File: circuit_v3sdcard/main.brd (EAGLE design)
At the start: 28 x 47 mm, 30 parts, among them CN1 SD, CN2 USB_BARE, CN3 MICROSD, IC1 C8051F381-GM, IC3 N25Q512A, IC4 KC2016K, IC6 MPU-9250, P0.0 PTR1TP10R, SW2 PTR1TP10R

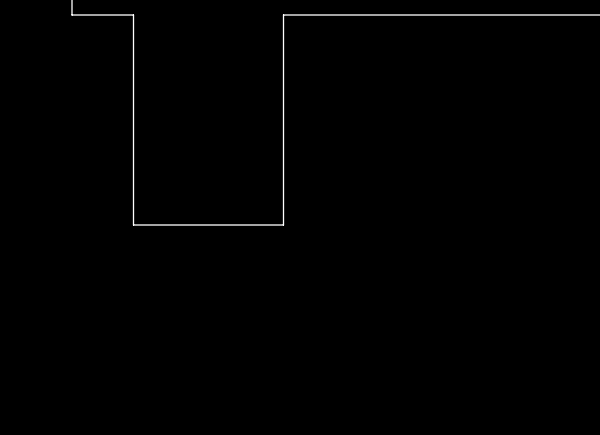
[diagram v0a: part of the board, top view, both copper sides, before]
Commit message: Added molex connector's library
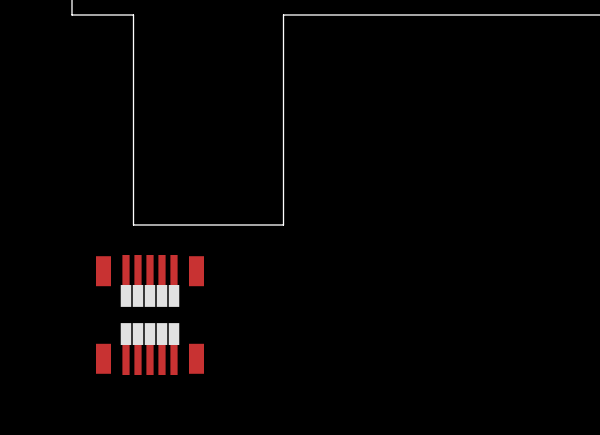
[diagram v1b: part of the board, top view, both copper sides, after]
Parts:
- added CN4: 5035481020, Connector:5035481020
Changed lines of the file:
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@@
 <element name="CN1" library="Connector" package="SD" value="SD" x="20.17" y="23.67" rot="MR0"/>
 <element name="CN3" library="Connector" package="BLOCK_SD_CONNECTOR" value="MICROSD" x="16" y="9"/>
+<element name="CN4" library="Connector" package="5035481020" value="5035481020" x="3" y="-3"/>
 </elements>
 <signals>

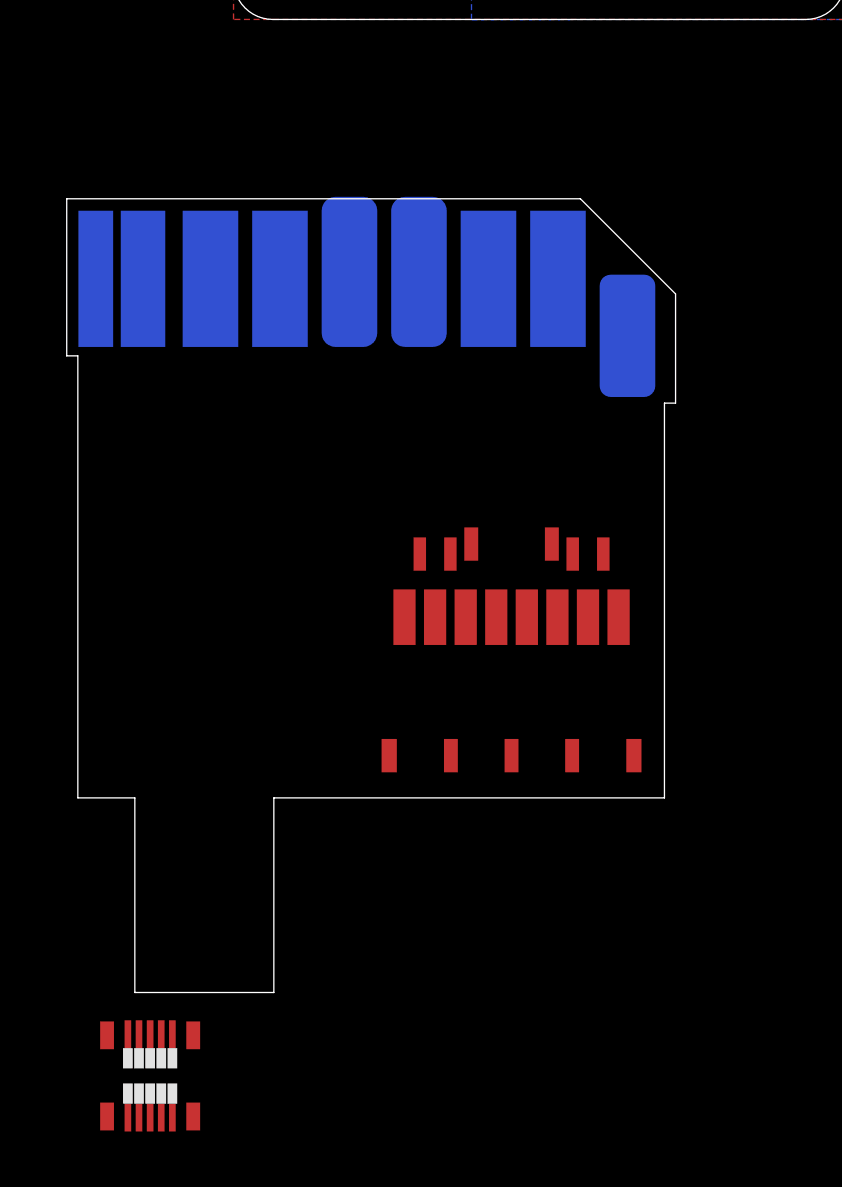
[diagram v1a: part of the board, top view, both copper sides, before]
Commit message: Modified Contours
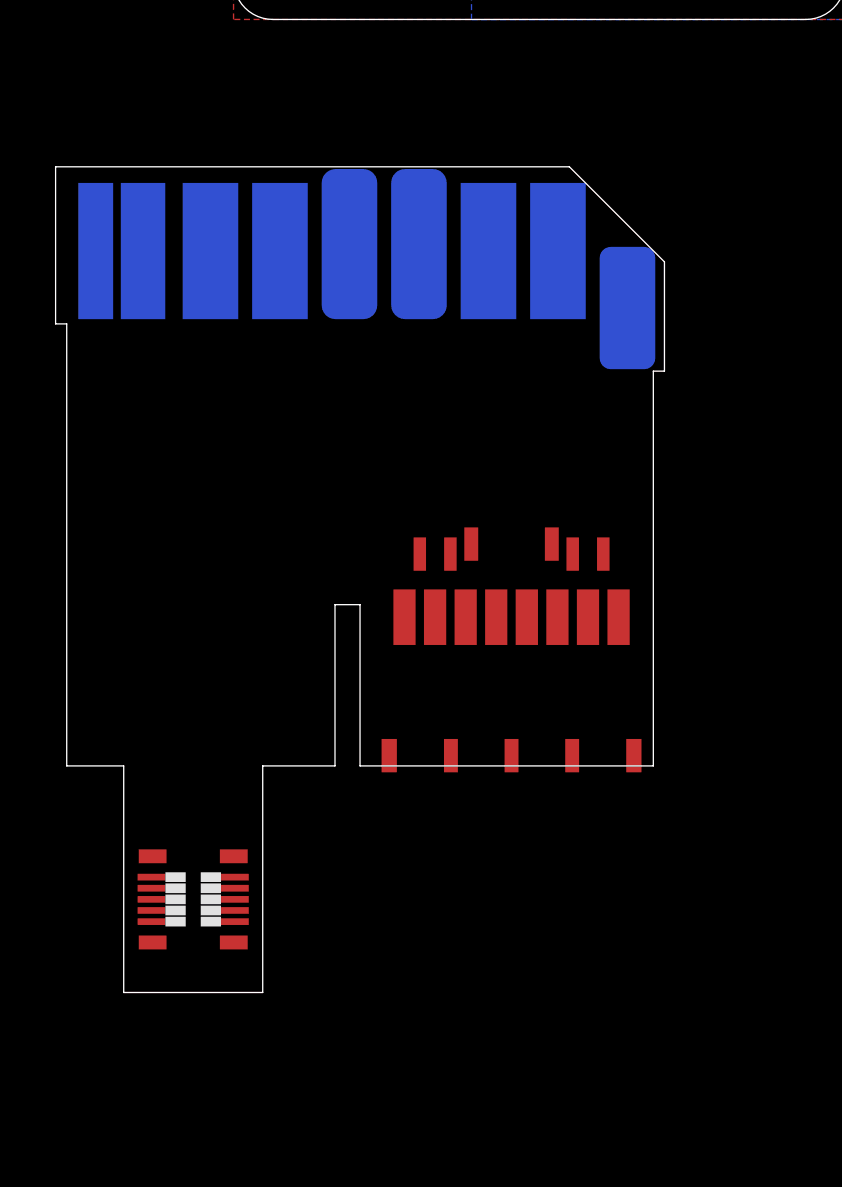
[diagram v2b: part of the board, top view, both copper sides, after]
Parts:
- moved CN4 6.54 mm to (4.55, 3.35), turned to 90 degrees
- moved CN1 1.00 mm to (20.2, 24.7)
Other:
- board size 28 x 47 mm -> 28.4 x 47 mm
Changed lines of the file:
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@@
 <text x="14.4" y="38.39" size="0.8128" layer="26" font="vector" ratio="12" rot="SMR0">Designed by</text>
 <text x="14.44" y="35.89" size="0.8128" layer="26" font="vector" ratio="12" rot="SMR0">Y. Sato</text>
-<wire x1="2.45" y1="0" x2="2.45" y2="7" width="0" layer="20"/>
-<wire x1="2.45" y1="7" x2="0.4" y2="7" width="0" layer="20"/>
-<wire x1="0.4" y1="7" x2="0.4" y2="22.9" width="0" layer="20"/>
-<wire x1="0.4" y1="22.9" x2="0" y2="22.9" width="0" layer="20"/>
-<wire x1="0" y1="22.9" x2="0" y2="28.55" width="0" layer="20"/>
-<wire x1="0" y1="28.55" x2="18.477" y2="28.55" width="0" layer="20"/>
-<wire x1="18.477" y1="28.55" x2="21.9" y2="25.127" width="0" layer="20"/>
-<wire x1="21.9" y1="25.127" x2="21.9" y2="21.2" width="0" layer="20"/>
-<wire x1="21.9" y1="21.2" x2="21.5" y2="21.2" width="0" layer="20"/>
-<wire x1="21.5" y1="21.2" x2="21.5" y2="7" width="0" layer="20"/>
-<wire x1="21.5" y1="7" x2="7.45" y2="7" width="0" layer="20"/>
-<wire x1="7.45" y1="7" x2="7.45" y2="0" width="0" layer="20"/>
-<wire x1="7.45" y1="0" x2="2.45" y2="0" width="0" layer="20"/>
+<wire x1="2.05" y1="0" x2="2.05" y2="8.15" width="0" layer="20"/>
+<wire x1="2.05" y1="8.15" x2="0" y2="8.15" width="0" layer="20"/>
+<wire x1="0" y1="8.15" x2="0" y2="24.05" width="0" layer="20"/>
+<wire x1="0" y1="24.05" x2="-0.4" y2="24.05" width="0" layer="20"/>
+<wire x1="-0.4" y1="24.05" x2="-0.4" y2="29.7" width="0" layer="20"/>
+<wire x1="-0.4" y1="29.7" x2="18.08" y2="29.7" width="0" layer="20"/>
+<wire x1="18.08" y1="29.7" x2="21.5" y2="26.28" width="0" layer="20"/>
+<wire x1="21.5" y1="26.28" x2="21.5" y2="22.35" width="0" layer="20"/>
+<wire x1="21.5" y1="22.35" x2="21.1" y2="22.35" width="0" layer="20"/>
+<wire x1="21.1" y1="22.35" x2="21.1" y2="8.15" width="0" layer="20"/>
+<wire x1="21.1" y1="8.15" x2="10.55" y2="8.15" width="0" layer="20"/>
+<wire x1="9.65" y1="8.15" x2="7.05" y2="8.15" width="0" layer="20"/>
+<wire x1="7.05" y1="8.15" x2="7.05" y2="0" width="0" layer="20"/>
+<wire x1="7.05" y1="0" x2="2.05" y2="0" width="0" layer="20"/>
+<wire x1="10.55" y1="8.15" x2="10.55" y2="13.95" width="0" layer="20"/>
+<wire x1="10.55" y1="13.95" x2="9.65" y2="13.95" width="0" layer="20"/>
+<wire x1="9.65" y1="13.95" x2="9.65" y2="8.15" width="0" layer="20"/>
 </plain>
 <attributes>
@@
 <attribute name="VALUE" x="21.615" y="41.225" size="1.27" layer="28" rot="MR0"/>
 </element>
-<element name="CN1" library="Connector" package="SD" value="SD" x="20.17" y="23.67" rot="MR0"/>
+<element name="CN1" library="Connector" package="SD" value="SD" x="20.17" y="24.67" rot="MR0"/>
 <element name="CN3" library="Connector" package="BLOCK_SD_CONNECTOR" value="MICROSD" x="16" y="9"/>
-<element name="CN4" library="Connector" package="5035481020" value="5035481020" x="3" y="-3"/>
+<element name="CN4" library="Connector" package="5035481020" value="5035481020" x="4.55" y="3.35" rot="R90"/>
 </elements>
 <signals>

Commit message: Modified circuit
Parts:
- moved CN3 0.83 mm to (15.7, 8.23)
- moved CN4 0.50 mm to (4.55, 2.85)
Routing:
- added copper zone on layer 1, net DGND
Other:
- outline, holes or cut-outs redrawn
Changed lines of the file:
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@@
 <text x="14.4" y="38.39" size="0.8128" layer="26" font="vector" ratio="12" rot="SMR0">Designed by</text>
 <text x="14.44" y="35.89" size="0.8128" layer="26" font="vector" ratio="12" rot="SMR0">Y. Sato</text>
-<wire x1="2.05" y1="0" x2="2.05" y2="8.15" width="0" layer="20"/>
-<wire x1="2.05" y1="8.15" x2="0" y2="8.15" width="0" layer="20"/>
-<wire x1="0" y1="8.15" x2="0" y2="24.05" width="0" layer="20"/>
+<wire x1="2.05" y1="0" x2="2.05" y2="7.15" width="0" layer="20"/>
+<wire x1="2.05" y1="7.15" x2="0" y2="7.15" width="0" layer="20"/>
+<wire x1="0" y1="7.15" x2="0" y2="24.05" width="0" layer="20"/>
 <wire x1="0" y1="24.05" x2="-0.4" y2="24.05" width="0" layer="20"/>
 <wire x1="-0.4" y1="24.05" x2="-0.4" y2="29.7" width="0" layer="20"/>
@@
 <wire x1="21.5" y1="26.28" x2="21.5" y2="22.35" width="0" layer="20"/>
 <wire x1="21.5" y1="22.35" x2="21.1" y2="22.35" width="0" layer="20"/>
-<wire x1="21.1" y1="22.35" x2="21.1" y2="8.15" width="0" layer="20"/>
-<wire x1="21.1" y1="8.15" x2="10.55" y2="8.15" width="0" layer="20"/>
-<wire x1="9.65" y1="8.15" x2="7.05" y2="8.15" width="0" layer="20"/>
-<wire x1="7.05" y1="8.15" x2="7.05" y2="0" width="0" layer="20"/>
+<wire x1="21.1" y1="22.35" x2="21.1" y2="6.85" width="0" layer="20"/>
+<wire x1="21.1" y1="6.85" x2="10.7" y2="6.85" width="0" layer="20"/>
+<wire x1="9.65" y1="7.15" x2="7.05" y2="7.15" width="0" layer="20"/>
+<wire x1="7.05" y1="7.15" x2="7.05" y2="0" width="0" layer="20"/>
 <wire x1="7.05" y1="0" x2="2.05" y2="0" width="0" layer="20"/>
-<wire x1="10.55" y1="8.15" x2="10.55" y2="13.95" width="0" layer="20"/>
-<wire x1="10.55" y1="13.95" x2="9.65" y2="13.95" width="0" layer="20"/>
-<wire x1="9.65" y1="13.95" x2="9.65" y2="8.15" width="0" layer="20"/>
+<wire x1="10.7" y1="6.85" x2="10.7" y2="17" width="0" layer="20"/>
+<wire x1="10.7" y1="17" x2="9.65" y2="17" width="0" layer="20"/>
+<wire x1="9.65" y1="17" x2="9.65" y2="7.15" width="0" layer="20"/>
 </plain>
 <attributes>
@@
 </element>
 <element name="CN1" library="Connector" package="SD" value="SD" x="20.17" y="24.67" rot="MR0"/>
-<element name="CN3" library="Connector" package="BLOCK_SD_CONNECTOR" value="MICROSD" x="16" y="9"/>
-<element name="CN4" library="Connector" package="5035481020" value="5035481020" x="4.55" y="3.35" rot="R90"/>
+<element name="CN3" library="Connector" package="BLOCK_SD_CONNECTOR" value="MICROSD" x="15.7" y="8.23"/>
+<element name="CN4" library="Connector" package="5035481020" value="5035481020" x="4.55" y="2.85" rot="R90"/>
 </elements>
 <signals>
@@
 <vertex x="14.56" y="34.99"/>
 </polygon>
+<polygon width="0.1524" layer="1">
+<vertex x="3" y="21"/>
+<vertex x="5" y="19"/>
+<vertex x="5" y="16"/>
+<vertex x="3" y="16"/>
+</polygon>
 </signal>

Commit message: Modified SD circuit
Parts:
- CN1: device Connector:SD -> Connector:SD_V3
- moved CN1 0.24 mm to (19.9, 24.7)
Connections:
- new net N$10: CN1.DI(CMD), CN3.CMD
- new net N$12: CN1.!CS!(DAT3), CN3.CD/DAT3
- new net N$14: CN1.RSV(DAT2), CN3.DAT2
- new net N$2: CN1.RSV(DAT1), CN3.DAT1
- new net N$3: CN1.DO(DAT0), CN3.DAT0
- new net N$4: CN1.VSS1, CN1.VSS2, CN3.VSS
- new net N$6: CN1.SCLK, CN3.CLK
- new net N$8: CN1.VDD, CN3.VDD
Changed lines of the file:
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@@
 <setting verticaltext="up"/>
 </settings>
-<grid distance="1" unitdist="mm" unit="mm" style="lines" multiple="1" display="yes" altdistance="0.01" altunitdist="mm" altunit="mm"/>
+<grid distance="0.5" unitdist="mm" unit="mm" style="lines" multiple="1" display="yes" altdistance="0.01" altunitdist="mm" altunit="mm"/>
 <layers>
 <layer number="1" name="Top" color="4" fill="1" visible="yes" active="yes"/>
@@
 </variantdefs>
 <classes>
-<class number="0" name="default" width="0" drill="0">
+<class number="0" name="signal" width="0.1524" drill="0">
+</class>
+<class number="1" name="power" width="0.254" drill="0">
 </class>
 </classes>
@@
 <attribute name="VALUE" x="21.615" y="41.225" size="1.27" layer="28" rot="MR0"/>
 </element>
-<element name="CN1" library="Connector" package="SD" value="SD" x="20.17" y="24.67" rot="MR0"/>
+<element name="CN1" library="Connector" package="SD_V3" value="SD" x="19.93" y="24.68" rot="MR0"/>
 <element name="CN3" library="Connector" package="BLOCK_SD_CONNECTOR" value="MICROSD" x="15.7" y="8.23"/>
 <element name="CN4" library="Connector" package="5035481020" value="5035481020" x="4.55" y="2.85" rot="R90"/>
@@
 <wire x1="14.255" y1="44.545" x2="14.255" y2="44.3" width="0.1524" layer="1"/>
 </signal>
+<signal name="N$2">
+<contactref element="CN3" pad="DAT1"/>
+<contactref element="CN1" pad="RSV(DAT1)"/>
+<wire x1="11.3" y1="7.8" x2="0.81" y2="26.88" width="0" layer="19" extent="1-16"/>
+</signal>
+<signal name="N$3">
+<contactref element="CN1" pad="DO(DAT0)"/>
+<contactref element="CN3" pad="DAT0"/>
+<wire x1="12.4" y1="15" x2="2.51" y2="26.88" width="0" layer="19" extent="1-16"/>
+</signal>
+<signal name="N$4">
+<contactref element="CN3" pad="VSS"/>
+<contactref element="CN1" pad="VSS2"/>
+<contactref element="CN1" pad="VSS1"/>
+<wire x1="4.93" y1="26.88" x2="12.43" y2="26.98" width="0" layer="19" extent="16-16"/>
+<wire x1="13.5" y1="15" x2="12.43" y2="26.98" width="0" layer="19" extent="1-16"/>
+</signal>
+<signal name="N$6">
+<contactref element="CN1" pad="SCLK"/>
+<contactref element="CN3" pad="CLK"/>
+<wire x1="14.25" y1="15.36" x2="7.43" y2="26.88" width="0" layer="19" extent="1-16"/>
+</signal>
+<signal name="N$8">
+<contactref element="CN3" pad="VDD"/>
+<contactref element="CN1" pad="VDD"/>
+<wire x1="17.15" y1="15.36" x2="9.93" y2="26.98" width="0" layer="19" extent="1-16"/>
+</signal>
+<signal name="N$10">
+<contactref element="CN1" pad="DI(CMD)"/>
+<contactref element="CN3" pad="CMD"/>
+<wire x1="17.9" y1="15" x2="14.93" y2="26.88" width="0" layer="19" extent="1-16"/>
+</signal>
+<signal name="N$12">
+<contactref element="CN1" pad="!CS!(DAT3)"/>
+<contactref element="CN3" pad="CD/DAT3"/>
+<wire x1="17.43" y1="26.88" x2="19" y2="15" width="0" layer="19" extent="1-16"/>
+</signal>
+<signal name="N$14">
+<contactref element="CN3" pad="DAT2"/>
+<contactref element="CN1" pad="RSV(DAT2)"/>
+<wire x1="20.1" y1="7.8" x2="19.93" y2="24.68" width="0" layer="19" extent="1-16"/>
+</signal>
 </signals>

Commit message: Modified v3 circuit
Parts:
- removed C2CK, C2D, DGND, GND, P0.0, SW2: PTR1TP10R, testpad:TP10R
- removed CN2: USB_BARE, Connector:USB_BARE
- removed HDMI_5V, HDMI_GND: PTR1TP11R, testpad:TP11R
- removed R3: 100, reg,cap:1005
- added D4: (no value), diode:SOD323-W
- added TP: PTR1TP10R, testpad:TP10R
- added USB_GND: PTR1TP11R, testpad:TP11R
- R1: value 100k -> 10k
- moved R1 61.5 mm to (1.00, -15.0), flipped to the top
- moved D1 54.7 mm to (2.00, -7.00), flipped to the top
- moved D2 52.8 mm to (2.00, -3.00), flipped to the top, turned to 0 degrees
- moved D3 21.5 mm to (19.0, 19.5), flipped to the top
- moved R7 6.58 mm to (22.0, 30.5), flipped to the top
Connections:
- net IN renamed N$4
- removed net N$1: IC1.25, SW2.TP
- removed net N$18: IC1.8, R3.P$2
- removed net N$4 (its old number): CN1.VSS1, CN1.VSS2, CN3.VSS
- removed net N$7: D2.A, HDMI_5V.TP
- removed net N$8: CN1.VDD, CN3.VDD
- new net GPIO0: CN4.5, IC1.26
- new net GPIO1: CN4.7, IC1.25
- new net N$5: D4.C, IC1.8, R1.P$2
- new net RX1: CN4.3, IC1.1
- new net TX1: CN4.1, IC1.2
- net +3V3: now also CN1.VDD, CN3.VDD, D2.A
- net C2CK: now also CN4.9; no longer C2CK.TP
- net C2D: now also CN4.10; no longer C2D.TP
- net D+: now also CN4.6; no longer CN2.3
- net D-: now also CN4.4; no longer CN2.2
- net DGND: now also CN1.VSS1, CN1.VSS2, CN3.VSS, CN4.8, USB_GND.TP; no longer CN2.4, DGND.TP, GND.TP, HDMI_GND.TP
- net N$15: now also TP.TP; no longer P0.0.TP
- net VBUS: now also CN4.2, D4.A; no longer CN2.1, R1.P$2, R3.P$1
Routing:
- net VBUS: track 13.0 -> 0.71 mm
- net N$15: track 8.14 -> 19.6 mm
- net D+: track 10.9 -> 4.61 mm
- net D-: track 12.4 -> 6.85 mm
- net N$9: track 3.01 -> 8.05 mm
- net N$4: track 11.8 -> 8.93 mm
- net N$7: track 2.24 -> 0.00 mm
- net N$18: track 2.06 -> 0.00 mm, vias 1 -> 0
- net C2CK: track 6.04 -> 4.76 mm
- net DGND: track 35.8 -> 34.6 mm, vias 9 -> 8
- net N$1: track 1.09 -> 0.00 mm
- net C2D: track 7.82 -> 7.13 mm
- removed copper zone on layer 1, net DGND
- removed copper zone on layer 16, net DGND
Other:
- board size 28.4 x 47 mm -> 21.7 x 29.5 mm

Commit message: Modified v3 circuit
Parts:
- removed D1, D2: (no value), diode:SOD323-W
- removed LED1: (no value), LED:1608-OLI
- removed R7: 10k, reg,cap:1005
- removed TP: PTR1TP10R, testpad:TP10R
- removed USB_GND: PTR1TP11R, testpad:TP11R
- D4: value (none) -> HSMS-2854; device diode:SOD323-W -> avago:SOT23
- moved C9 32.4 mm to (16.3, 68.7), turned to 0 degrees
- moved R26 32.1 mm to (16.5, 70.0), turned to 0 degrees
- moved IC3 31.3 mm to (23.0, 69.5), turned to 180 degrees
- moved R2 30.6 mm to (1.62, 15.7), turned to 0 degrees
- moved C10 24.8 mm to (16.8, 60.9), turned to 90 degrees
- moved IC4 24.0 mm to (15.0, 60.9), turned to 270 degrees
- moved D3 19.5 mm to (2.00, 10.0)
- moved C6 18.1 mm to (12.6, 54.0)
- moved R1 16.8 mm to (8.50, 0.00)
- moved D4 16.6 mm to (10.0, 3.50)
- moved IC1 12.0 mm to (17.6, 54.5), turned to 0 degrees
- moved C3 7.06 mm to (19.0, 43.0), turned to 90 degrees
- moved IC6 6.31 mm to (19.0, 47.0)
- moved C2 6.31 mm to (18.0, 43.0)
- moved C4 6.00 mm to (23.0, 46.0), turned to 180 degrees
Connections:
- removed net N$15: IC1.11, R7.P$2, TP.TP
- removed net N$4: D1.C, D2.C, IC1.7
- removed net N$5: D4.C, IC1.8, R1.P$2
- removed net N$9: LED1.A, R7.P$1
- new net N$1: D4.3, IC1.7
- net +3V3: now also D4.2; no longer D2.A
- net DGND: no longer LED1.K, USB_GND.TP
- net VBUS: now also D4.1, IC1.8, R1.P$2; no longer D1.A, D4.A
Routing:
- net DGND: track 34.6 -> 0.00 mm, vias 8 -> 0
- net N$15: track 19.6 -> 0.00 mm, vias 1 -> 0
- net EEPROM_MOSI: track 10.7 -> 0.00 mm
- net N$11: track 10.6 -> 0.00 mm
- net EEPROM_SCK: track 10.2 -> 0.00 mm
- net N$4: track 8.93 -> 0.00 mm, vias 1 -> 0
- net N$9: track 8.05 -> 0.00 mm, vias 1 -> 0
- net IMU_!CS: track 7.53 -> 0.00 mm
- net IMU_MISO: track 7.44 -> 0.00 mm, vias 2 -> 0
- net IMU_SCK: track 7.18 -> 0.00 mm
- net C2D: track 7.13 -> 0.00 mm
- net D-: track 6.85 -> 0.00 mm, vias 1 -> 0
- net IMU_MOSI: track 6.82 -> 0.00 mm
- net EEPROM_MISO: track 5.06 -> 0.00 mm
- net C2CK: track 4.76 -> 0.00 mm
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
